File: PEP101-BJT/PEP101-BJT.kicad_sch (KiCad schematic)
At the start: 13 parts, among them J1 Screw_Terminal_01x02, J2 Screw_Terminal_01x02, J3 Screw_Terminal_01x02, Q2 MMBT5551L

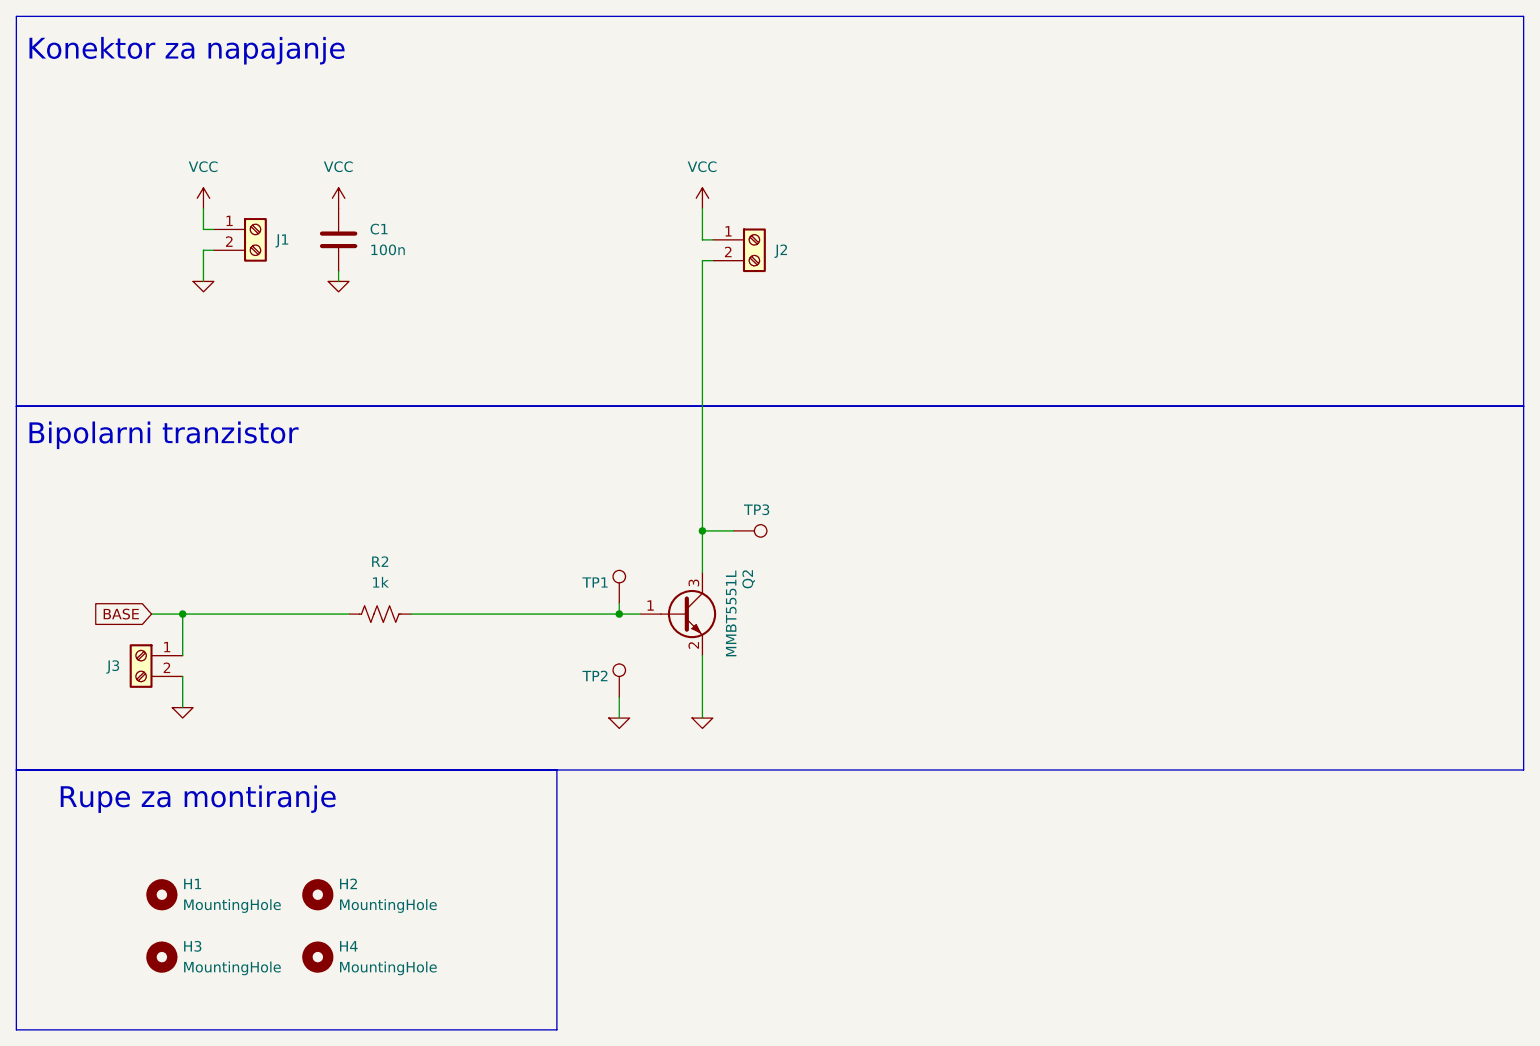
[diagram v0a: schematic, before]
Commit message: bjt and mosfet need to be redesigned.
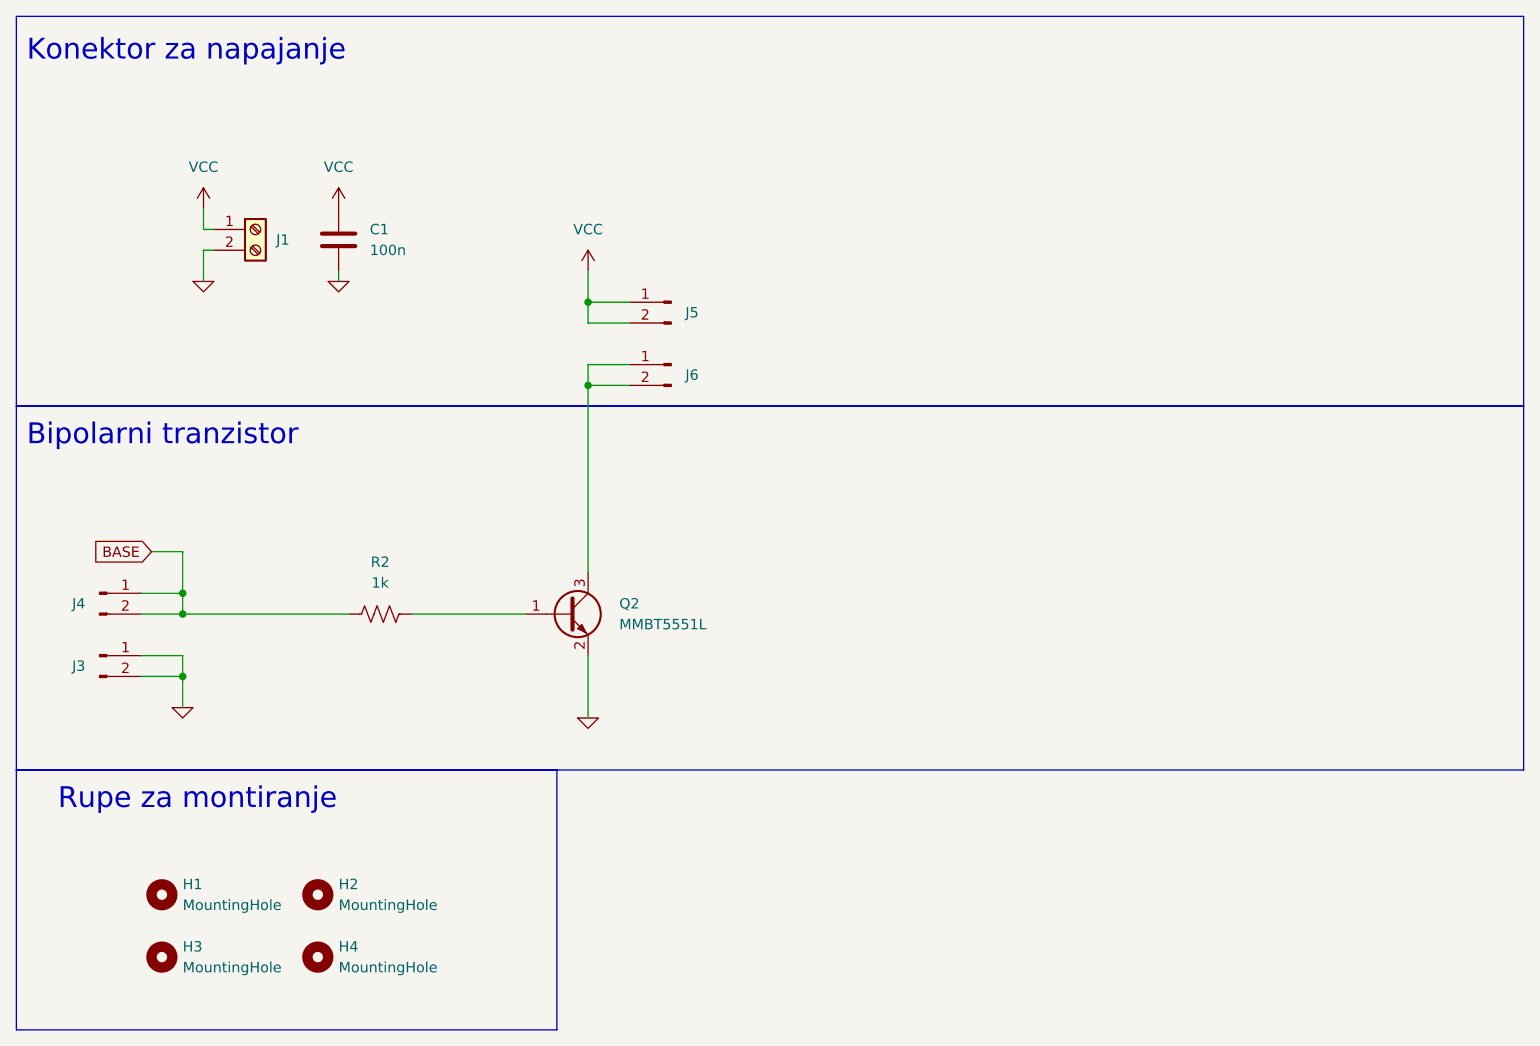
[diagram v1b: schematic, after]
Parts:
- removed J2: Screw_Terminal_01x02, PEP_library:Screw terminal, symbol PEP_library:Screw_Terminal_01x02
- removed J3: Screw_Terminal_01x02, PEP_library:TerminalBlock_Phoenix_MKDS-1,5-2-5.08_1x02_P5.08mm_Horizontal, symbol PEP_library:Screw_Terminal_01x02
- removed TP1, TP2, TP3: TestPoint, TestPoint:TestPoint_Pad_D4.0mm, symbol Connector:TestPoint
- added J3, J4, J5, J6: Conn_01x02_Pin, Connector_PinHeader_2.54mm:PinHeader_2x01_P2.54mm_Vertical, symbol Connector:Conn_01x02_Pin
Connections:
- net 0: now also J3.1 (Pin_1), J3.2 (Pin_2)
- net BASE: now also J4.1 (Pin_1), J4.2 (Pin_2)
- net VCC: now also J5.1 (Pin_1), J5.2 (Pin_2)
- net at Q2.3 (C): now also J6.1 (Pin_1), J6.2 (Pin_2)
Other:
- moved on the sheet: Q2
